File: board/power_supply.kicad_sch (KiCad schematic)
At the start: 21 parts

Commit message: updated schematic after review
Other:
- note added: "TODO: Further Power conditioning? Ferrit Bead mit Dämpfung bei Tackt-F von ESP Vor Linearregler? Danach? Domi-> Keine Ahnung"
- note removed: "TODO: Further Power conditioning?"
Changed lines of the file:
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@@
     (stroke (width 0) (type default) (color 0 0 0 0))
   )
-  (text "TODO: Further Power conditioning?" (at 170.18 101.6 0)
+  (text "TODO: Further Power conditioning?\nFerrit Bead mit Dämpfung bei Tackt-F von ESP\nVor Linearregler? Danach? Domi-> Keine Ahnung"
+    (at 170.18 101.6 0)
     (effects (font (size 1.27 1.27)) (justify left bottom))
   )

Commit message: updated schematic
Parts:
- added SW?: MAIN, symbol Switch:SW_SPST
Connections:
- net at BT?.1 (+): now also SW?.1 (A); no longer Q?.3 (D)
- new net: Q?.3 (D), SW?.2 (B)
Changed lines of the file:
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@@
+    (stroke (width 0) (type default) (color 0 0 0 0))
+  )
+  (wire (pts (xy 24.13 22.86) (xy 31.75 22.86))
     (stroke (width 0) (type default) (color 0 0 0 0))
   )
@@
     (stroke (width 0) (type default) (color 0 0 0 0))
   )
-  (wire (pts (xy 24.13 22.86) (xy 48.26 22.86))
-    (stroke (width 0) (type default) (color 0 0 0 0))
-  )
   (wire (pts (xy 24.13 60.96) (xy 24.13 62.23))
     (stroke (width 0) (type default) (color 0 0 0 0))
@@
   )
   (wire (pts (xy 237.49 120.65) (xy 237.49 121.92))
+    (stroke (width 0) (type default) (color 0 0 0 0))
+  )
+  (wire (pts (xy 41.91 22.86) (xy 48.26 22.86))
     (stroke (width 0) (type default) (color 0 0 0 0))
   )
@@
     (pin "1")
   )
+  (symbol (lib_id "Switch:SW_SPST") (at 36.83 22.86 0) (unit 1)
+    (in_bom yes) (on_board yes) (fields_autoplaced)
+    (property "Reference" "SW?" (id 0) (at 36.83 16.51 0))
+    (property "Value" "MAIN" (id 1) (at 36.83 19.05 0))
+    (property "Footprint" "" (id 2) (at 36.83 22.86 0)
+      (effects (font (size 1.27 1.27)) hide)
+    )
+    (property "Datasheet" "~" (id 3) (at 36.83 22.86 0)
+      (effects (font (size 1.27 1.27)) hide)
+    )
+    (pin "1")
+    (pin "2")
+  )
   (symbol (lib_id "Device:R") (at 53.34 42.545 0) (mirror y) (unit 1)

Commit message: updated schematic
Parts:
- added FB? (x2): BLM15BB, symbol Device:FerriteBead_Small
- added Q? (x2): BSH203,215, Package_TO_SOT_SMD:SOT-23, symbol Device:Q_PMOS_GSD
- added R? (x2): 10k, Resistor_SMD:R_0402_1005Metric, symbol Device:R
- added R? (x2): 100R, Resistor_SMD:R_0402_1005Metric, symbol Device:R
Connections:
- net +3.3VA: now also FB?.1; no longer C?.1, C?.1, U?.1 (OUT)
- net +3V3: now also Q?.2 (S), R?.2
- net +5V: now also Q?.2 (S), R?.2
- net +5VA: now also FB?.1; no longer C?.1, C?.1, C?.1, U?.3 (VOUT)
- new net: Q?.1 (G), R?.1, R?.2 (x2)
- new net: C?.1, C?.1, C?.1, FB?.2, U?.3 (VOUT)
- new net: C?.1, C?.1, FB?.2, U?.1 (OUT)
- new net 3V3SW: Q?.3 (D)
- new net 5VSW: Q?.3 (D)
- new net SIG_SW: R?.1, R?.1
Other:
- note added: "I2C devices power switching"
- note removed: "TODO: Further Power conditioning? Ferrit Bead mit Dämpfung bei Tackt-F von ESP Vor Linearregler? Danach? Domi-> Keine Ahnung"
- moved on the sheet: C?, U?

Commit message: ERC run
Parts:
- gave numbers to parts that had none: 30

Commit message: updated schematic after review
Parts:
- R20, R23: value 10k -> 100k
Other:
- note added: "TODO: PTC Fuse"
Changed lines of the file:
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@@
     (stroke (width 0) (type default) (color 0 0 0 0))
+  )
+  (text "TODO: PTC Fuse" (at 53.34 63.5 0)
+    (effects (font (size 1.27 1.27)) (justify left bottom))
   )
   (text "I2C devices power switching" (at 13.97 152.4 0)
@@
       (effects (font (size 1.27 1.27)) (justify right))
     )
-    (property "Value" "10k" (id 1) (at 102.87 170.1799 0)
+    (property "Value" "100k" (id 1) (at 102.87 170.1799 0)
       (effects (font (size 1.27 1.27)) (justify right))
     )
@@
       (effects (font (size 1.27 1.27)) (justify right))
     )
-    (property "Value" "10k" (id 1) (at 44.45 170.1799 0)
+    (property "Value" "100k" (id 1) (at 44.45 170.1799 0)
       (effects (font (size 1.27 1.27)) (justify right))
     )

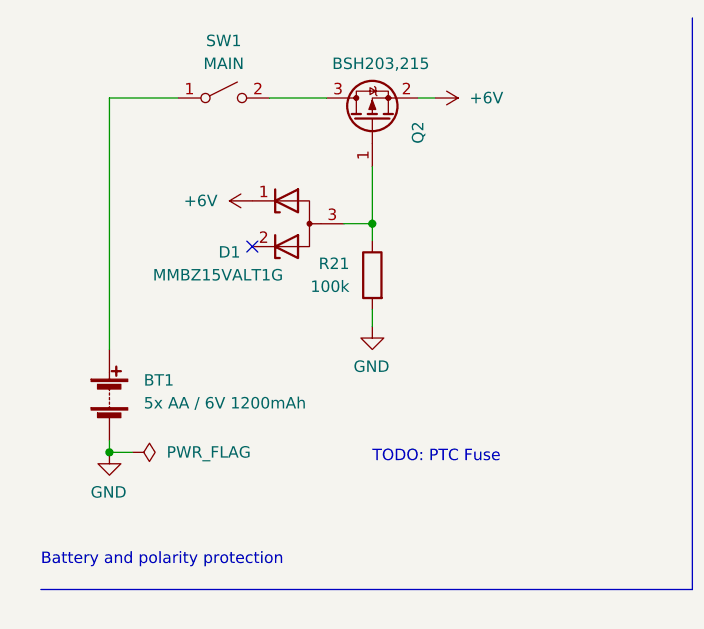
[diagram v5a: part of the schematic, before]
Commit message: added fuse and capacitor to schematic
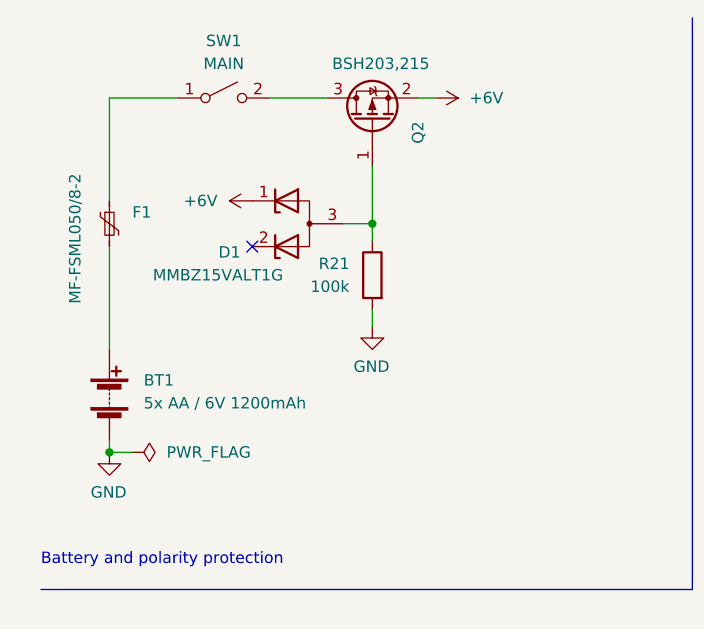
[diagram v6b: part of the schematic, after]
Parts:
- added F1: MF-FSML050/8-2, symbol Device:Polyfuse_Small
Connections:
- net at BT1.1 (+): now also F1.2; no longer SW1.1 (A)
- new net: F1.1, SW1.1 (A)
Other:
- note removed: "TODO: PTC Fuse"
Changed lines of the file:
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@@
     (stroke (width 0) (type solid) (color 0 0 0 0))
-  )
-  (wire (pts (xy 24.13 50.8) (xy 24.13 22.86))
-    (stroke (width 0) (type default) (color 0 0 0 0))
   )
   (wire (pts (xy 135.89 35.56) (xy 143.51 35.56))
@@
     (stroke (width 0) (type default) (color 0 0 0 0))
   )
+  (wire (pts (xy 24.13 22.86) (xy 24.13 34.29))
+    (stroke (width 0) (type default) (color 0 0 0 0))
+  )
   (wire (pts (xy 214.63 54.61) (xy 228.6 54.61))
     (stroke (width 0) (type default) (color 0 0 0 0))
@@
     (stroke (width 0) (type solid) (color 0 0 0 0))
   )
+  (wire (pts (xy 24.13 39.37) (xy 24.13 50.8))
+    (stroke (width 0) (type default) (color 0 0 0 0))
+  )
   (wire (pts (xy 250.19 54.61) (xy 250.19 55.88))
     (stroke (width 0) (type default) (color 0 0 0 0))
@@
   (wire (pts (xy 214.63 52.07) (xy 214.63 54.61))
     (stroke (width 0) (type default) (color 0 0 0 0))
-  )
-  (text "TODO: PTC Fuse" (at 53.34 63.5 0)
-    (effects (font (size 1.27 1.27)) (justify left bottom))
   )
   (text "I2C devices power switching" (at 13.97 152.4 0)
@@
     (pin "1")
   )
+  (symbol (lib_id "Device:Polyfuse_Small") (at 24.13 36.83 0) (unit 1)
+    (in_bom yes) (on_board yes)
+    (property "Reference" "F1" (id 0) (at 26.67 35.5599 0)
+      (effects (font (size 1.27 1.27)) (justify left))
+    )
+    (property "Value" "MF-FSML050/8-2" (id 1) (at 20.32 45.72 90)
+      (effects (font (size 1.27 1.27)) (justify left))
+    )
+    (property "Footprint" "" (id 2) (at 25.4 41.91 0)
+      (effects (font (size 1.27 1.27)) (justify left) hide)
+    )
+    (property "Datasheet" "~" (id 3) (at 24.13 36.83 0)
+      (effects (font (size 1.27 1.27)) hide)
+    )
+    (pin "1")
+    (pin "2")
+  )
   (symbol (lib_id "power:PWR_FLAG") (at 55.88 182.88 270) (unit 1)

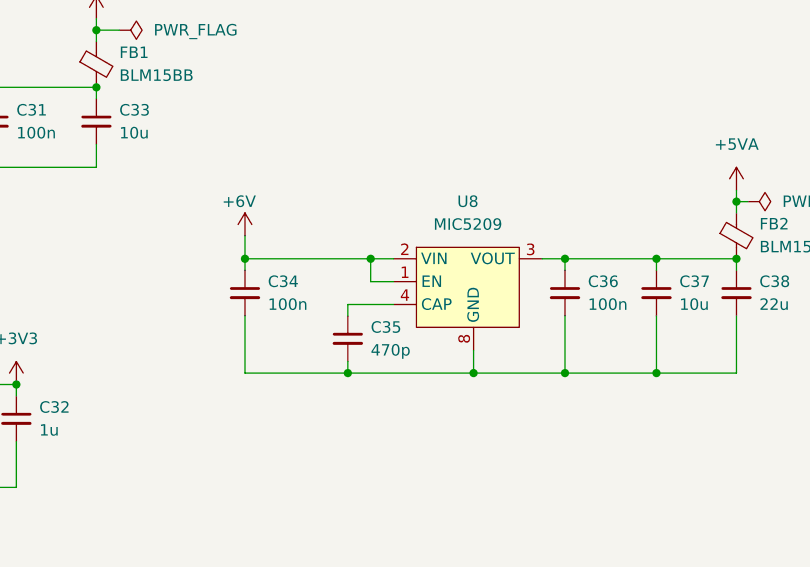
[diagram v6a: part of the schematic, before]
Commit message: added footprints to symbols and started layout
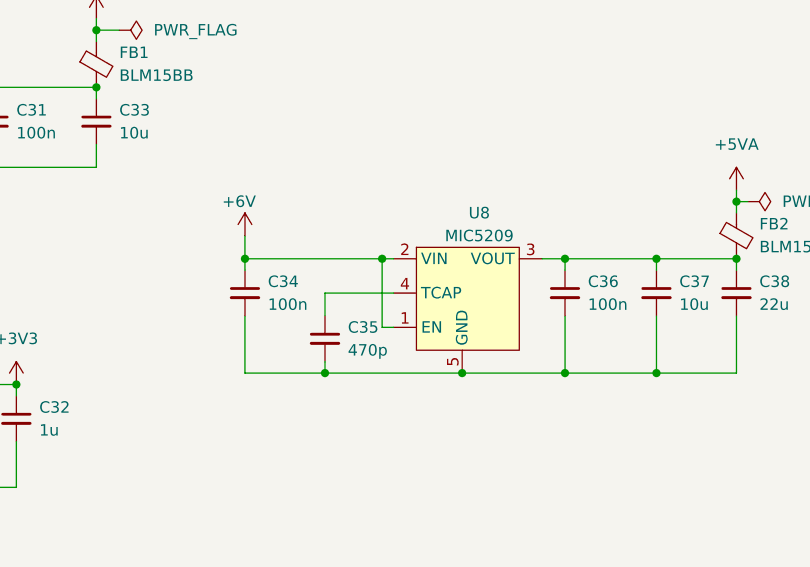
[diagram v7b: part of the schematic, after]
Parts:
- BT1, SW1: footprint (none) -> Connector_PinHeader_2.54mm:PinHeader_1x02_P2.54mm_Vertical
- C26, C27, C28, C30, C32, C33, C37: footprint (none) -> Capacitor_SMD:C_0603_1608Metric
- C29, C31, C34, C35, C36, FB1, FB2: footprint (none) -> Capacitor_SMD:C_0402_1005Metric
- C38: footprint (none) -> Capacitor_SMD:C_0805_2012Metric
- F1: footprint (none) -> ownLib:MF-FSML
- U5: footprint (none) -> Package_TO_SOT_SMD:SOT-223
- U6: footprint (none) -> Package_DFN_QFN:DFN-8-1EP_3x3mm_P0.65mm_EP1.7x2.05mm
- U7: footprint (none) -> Package_TO_SOT_SMD:TSOT-23-5
- U8: footprint (none) -> ownLib:SOICN-8LD; symbol ownLib:MIC5209 -> ownLib:MIC5209/YM
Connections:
- net GND: now also U6.9 (GND); no longer U6.EP (GND)
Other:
- moved on the sheet: C35, U8

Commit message: WIP pushed for meeting
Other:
- note added: "Disable Power?"
- note added: "Use FSML075 or FSML100 instead?"
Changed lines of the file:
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@@
     (stroke (width 0) (type default) (color 0 0 0 0))
+  )
+  (text "Disable Power?" (at 207.01 74.93 0)
+    (effects (font (size 1.27 1.27)) (justify left bottom))
   )
   (text "I2C devices power switching" (at 13.97 152.4 0)
@@
     (effects (font (size 1.27 1.27)) (justify left bottom))
   )
+  (text "Use FSML075 or FSML100 instead?" (at 17.78 53.34 90)
+    (effects (font (size 1.27 1.27)) (justify left bottom))
+  )
